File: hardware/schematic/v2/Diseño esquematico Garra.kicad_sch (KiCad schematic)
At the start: 21 parts, among them U2 ESP32-WROOM-32

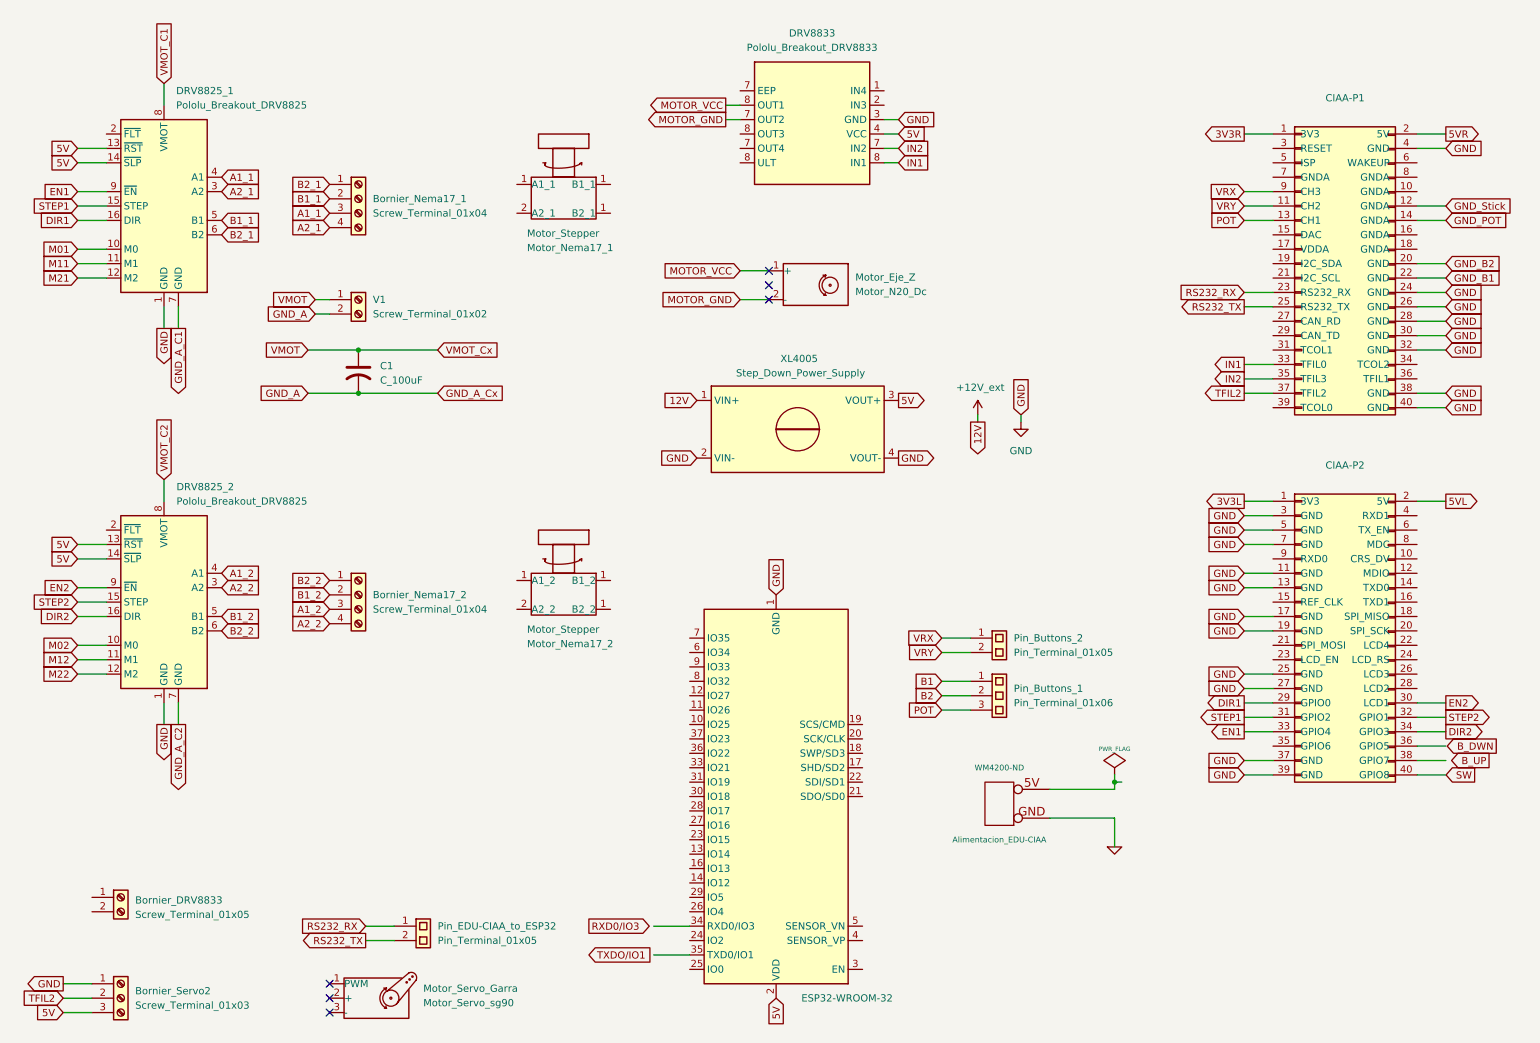
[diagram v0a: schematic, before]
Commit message: Added footprints to Schematic
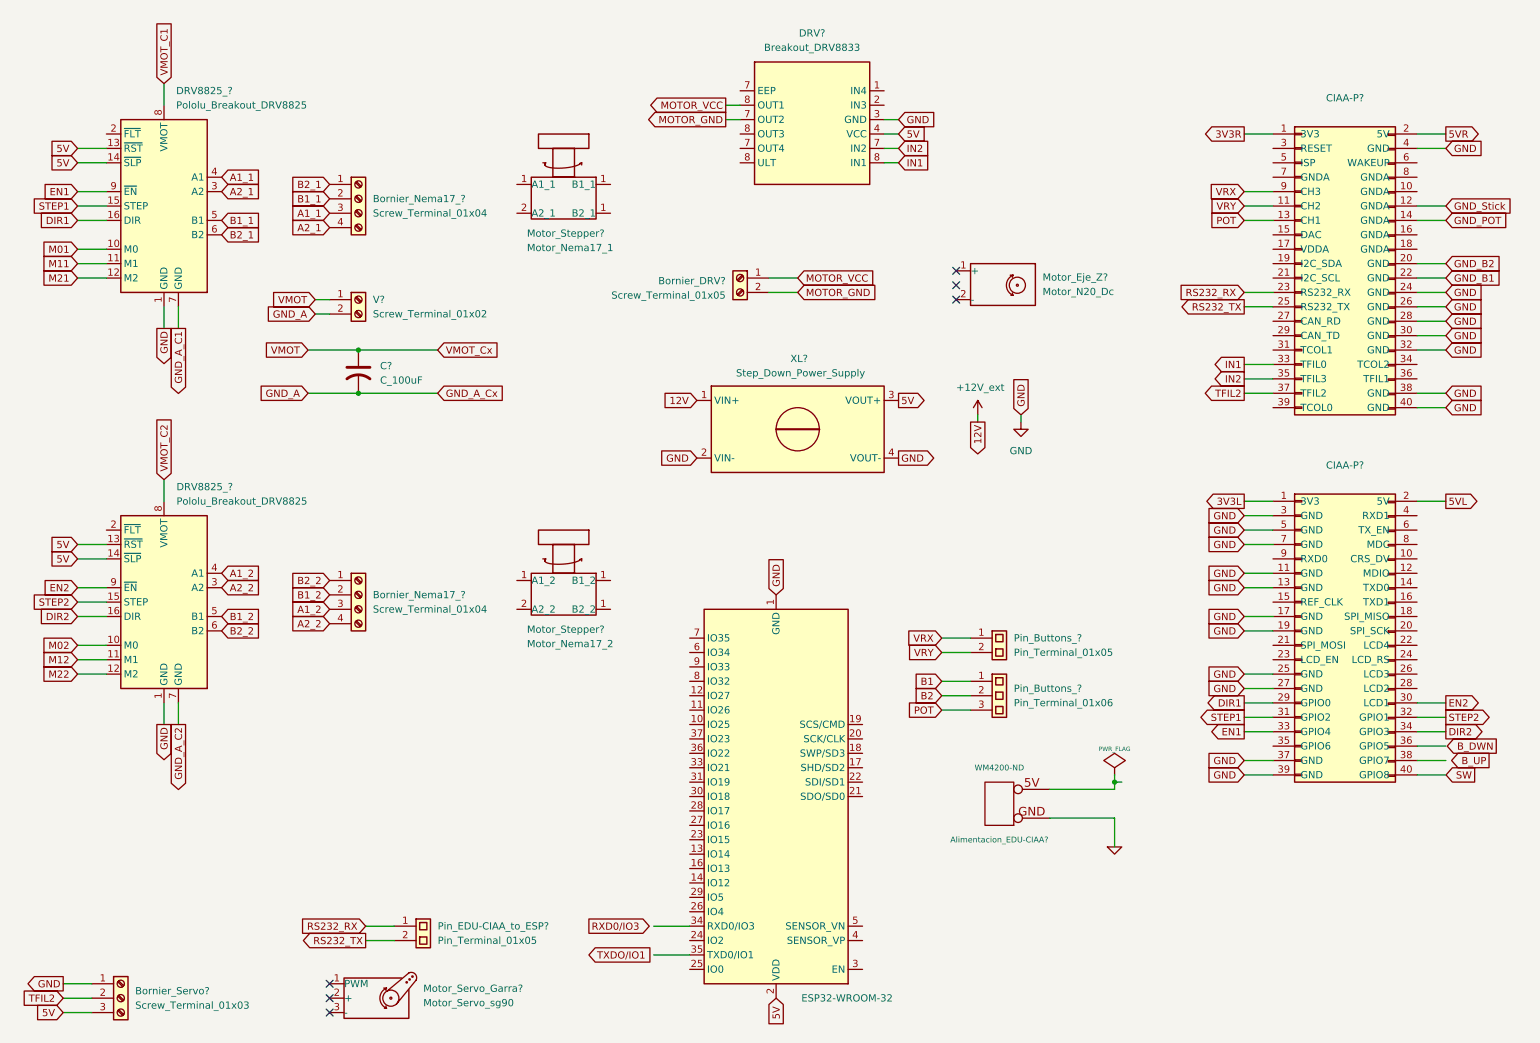
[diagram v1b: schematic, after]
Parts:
- Bornier_DRV?: renamed from Bornier_DRV8833; footprint ProyectoTdL:TerminalBlock_bornier-2_P5.08mm -> TerminalBlock_Phoenix:TerminalBlock_Phoenix_MKDS-1,5-2-5.08_1x02_P5.08mm_Horizontal
- Bornier_Nema17_?: renamed from Bornier_Nema17_1; footprint ProyectoTdL:TerminalBlock_bornier-4_P5.08mm -> TerminalBlock_Phoenix:TerminalBlock_Phoenix_MKDS-1,5-4-5.08_1x04_P5.08mm_Horizontal
- Bornier_Nema17_?: renamed from Bornier_Nema17_2; footprint ProyectoTdL:TerminalBlock_bornier-4_P5.08mm -> TerminalBlock_Phoenix:TerminalBlock_Phoenix_MKDS-1,5-4-5.08_1x04_P5.08mm_Horizontal
- Bornier_Servo?: renamed from Bornier_Servo2; footprint ProyectoTdL:TerminalBlock_bornier-3_P5.08mm -> TerminalBlock_Phoenix:TerminalBlock_Phoenix_MKDS-1,5-3-5.08_1x03_P5.08mm_Horizontal
- C?: renamed from C1; footprint (none) -> Capacitor_THT:C_Radial_D8.0mm_H11.5mm_P3.50mm
- DRV?: renamed from DRV8833; value Pololu_Breakout_DRV8833 -> Breakout_DRV8833
- V?: renamed from V1; footprint ProyectoTdL:TerminalBlock_bornier-2_P5.08mm -> TerminalBlock_Phoenix:TerminalBlock_Phoenix_MKDS-1,5-2-5.08_1x02_P5.08mm_Horizontal
- renumbered Alimentacion_EDU-CIAA to Alimentacion_EDU-CIAA?, CIAA-P1 to CIAA-P?, CIAA-P2 to CIAA-P?, DRV8825_2 to DRV8825_?, DRV8825_1 to DRV8825_?, Motor_Eje_Z to Motor_Eje_Z?, Motor_Servo_Garra to Motor_Servo_Garra?, Motor_Stepper to Motor_Stepper?, Pin_Buttons_2 to Pin_Buttons_?, Pin_Buttons_1 to Pin_Buttons_?, Pin_EDU-CIAA_to_ESP32 to Pin_EDU-CIAA_to_ESP?, U2 to U?, XL4005 to XL?
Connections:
- net MOTOR_GND: now also Bornier_DRV?.2 (Pin_2); no longer Motor_Eje_Z?.2 (-)
- net MOTOR_VCC: now also Bornier_DRV?.1 (Pin_1); no longer Motor_Eje_Z?.1 (+)
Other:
- moved on the sheet: Bornier_DRV?, Motor_Eje_Z?

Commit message: PCB started
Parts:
- removed Alimentacion_EDU-CIAA?: WM4200-ND, ~, symbol edu-ciaa-nxp:CONN_2
- removed Motor_Eje_Z?: Motor_N20_Dc, symbol Motor:Motor_Servo
- removed Motor_Servo_Garra?: Motor_Servo_sg90, symbol Motor:Motor_Servo
- removed Motor_Stepper?: Motor_Nema17_2, symbol Motor:Motor_Servo
- removed Motor_Stepper?: Motor_Nema17_1, symbol Motor:Motor_Servo
- removed U?: ESP32-WROOM-32, RF_Module:ESP32-WROOM-32, symbol RF_Module:ESP32-WROOM-32
- CIAA-P1: renamed from CIAA-P?; footprint ProyectoTdL:Tira_P1_CIAA -> Connector_PinHeader_1.00mm:PinHeader_1x20_P1.00mm_Vertical
- CIAA-P2: renamed from CIAA-P?; footprint ProyectoTdL:Tira_P2_CIAA -> Connector_PinHeader_1.00mm:PinHeader_1x20_P1.00mm_Vertical
- Pin_Buttons_?, Pin_EDU-CIAA_to_ESP?: footprint ProyectoTdL:TerminalBlock_bornier-2_P5.08mm -> Connector_PinSocket_2.00mm:PinSocket_1x02_P2.00mm_Vertical
- Pin_Buttons_?: footprint ProyectoTdL:TerminalBlock_bornier-3_P5.08mm -> Connector_PinSocket_2.00mm:PinSocket_1x03_P2.00mm_Vertical
- gave numbers to parts that had none: 7
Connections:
- net IN1: now also DRV8833.6 (IN1); no longer DRV8833.8 (IN1)
- net IN2: now also DRV8833.5 (IN2); no longer DRV8833.7 (IN2)
- net MOTOR_GND: now also DRV8833.9 (OUT2); no longer DRV8833.7 (IN2)
- no-connect marks 6 -> 0

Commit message: PCB progress
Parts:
- gave numbers to parts that had none: 6
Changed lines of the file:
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@@
 		(dnp no)
 		(fields_autoplaced yes)
-		(property "Reference" "Bornier_Nema17_?"
+		(property "Reference" "Bornier_Nema17_1"
 			(at 82.55 46.9899 0)
 			(effects
@@
 			(project "Diseño esquematico Garra"
 				(path "/a88248f6-7b70-4a9d-b538-4e8e42a3a066"
-					(reference "Bornier_Nema17_?")
+					(reference "Bornier_Nema17_1")
 					(unit 1)
 				)
@@
 		(dnp no)
 		(fields_autoplaced yes)
-		(property "Reference" "Pin_Buttons_?"
+		(property "Reference" "Pin_Buttons_1"
 			(at 195.58 124.4599 0)
 			(effects
@@
 			(project "Diseño esquematico Garra"
 				(path "/a88248f6-7b70-4a9d-b538-4e8e42a3a066"
-					(reference "Pin_Buttons_?")
+					(reference "Pin_Buttons_1")
 					(unit 1)
 				)
@@
 		(dnp no)
 		(fields_autoplaced yes)
-		(property "Reference" "Pin_Buttons_?"
+		(property "Reference" "Pin_Buttons_2"
 			(at 195.58 133.3499 0)
 			(effects
@@
 			(project "Diseño esquematico Garra"
 				(path "/a88248f6-7b70-4a9d-b538-4e8e42a3a066"
-					(reference "Pin_Buttons_?")
+					(reference "Pin_Buttons_2")
 					(unit 1)
 				)
@@
 		(dnp no)
 		(fields_autoplaced yes)
-		(property "Reference" "Bornier_Servo?"
+		(property "Reference" "Bornier_Servo1"
 			(at 40.64 186.6899 0)
 			(effects
@@
 			(project "Diseño esquematico Garra"
 				(path "/a88248f6-7b70-4a9d-b538-4e8e42a3a066"
-					(reference "Bornier_Servo?")
+					(reference "Bornier_Servo1")
 					(unit 1)
 				)
@@
 		(dnp no)
 		(fields_autoplaced yes)
-		(property "Reference" "Pin_EDU-CIAA_to_ESP?"
+		(property "Reference" "Pin_EDU-CIAA_to_ESP1"
 			(at 93.98 175.2599 0)
 			(effects
@@
 			(project "Diseño esquematico Garra"
 				(path "/a88248f6-7b70-4a9d-b538-4e8e42a3a066"
-					(reference "Pin_EDU-CIAA_to_ESP?")
+					(reference "Pin_EDU-CIAA_to_ESP1")
 					(unit 1)
 				)
@@
 		(dnp no)
 		(fields_autoplaced yes)
-		(property "Reference" "Bornier_Nema17_?"
+		(property "Reference" "Bornier_Nema17_2"
 			(at 82.55 116.8399 0)
 			(effects
@@
 			(project "Diseño esquematico Garra"
 				(path "/a88248f6-7b70-4a9d-b538-4e8e42a3a066"
-					(reference "Bornier_Nema17_?")
-					(unit 1)
-				)
+					(reference "Bornier_Nema17_2")
+					(unit 1)
+				)

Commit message: PCB Updated
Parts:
- removed Pin_Buttons_2: Pin_Terminal_01x06, Connector_PinSocket_2.00mm:PinSocket_1x03_P2.00mm_Vertical, symbol Connector:Screw_Terminal_01x03
- added C2: C_100uF, Capacitor_THT:C_Radial_D8.0mm_H11.5mm_P3.50mm, symbol Device:C_US
- added PinOut_B_DWN, PinOut_B_UP, PinOut_POT: Pin_Terminal_01x05, Connector_PinSocket_2.00mm:PinSocket_1x02_P2.00mm_Vertical, symbol Connector:Screw_Terminal_01x02
- CIAA-P1, CIAA-P2: footprint Connector_PinHeader_1.00mm:PinHeader_1x20_P1.00mm_Vertical -> Libreria_EDU_CIAA_NXP:PIN_ARRAY_20X2
- PinOut_Stick: renamed from Pin_Buttons_1; footprint Connector_PinSocket_2.00mm:PinSocket_1x02_P2.00mm_Vertical -> Connector_PinSocket_2.00mm:PinSocket_1x04_P2.00mm_Vertical
- renumbered Pin_EDU-CIAA_to_ESP1 to PinOut_UART, V1 to V_Input
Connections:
- net GND_A is gone; now on net GND: C1.2, V_Input.2 (Pin_2)
- net GND_A_C1 is gone; now on net GND: DRV8825_1.7 (GND)
- net GND_A_C2 is gone; now on net GND: DRV8825_2.7 (GND)
- net VMOT is gone; now on net +12V_ext: C1.1, V_Input.1 (Pin_1)
- net VMOT_C1 is gone; now on net +12V_ext: DRV8825_1.8 (VMOT)
- net VMOT_C2 is gone; now on net +12V_ext: DRV8825_2.8 (VMOT)
- net +12V_ext: now also C2.1
- net B_DWN: now also PinOut_B_DWN.1 (Pin_1)
- net B_UP: now also PinOut_B_UP.1 (Pin_1)
- net GND: now also C2.2
- net GND_POT: now also PinOut_POT.2 (Pin_2)
- net GND_Stick: now also PinOut_Stick.3 (Pin_3)
- net POT: now also PinOut_POT.1 (Pin_1)
- net SW: now also PinOut_Stick.4 (Pin_4)
- net GND_B1 renamed GND_B_DWN
- net GND_B_DWN: now also PinOut_B_DWN.2 (Pin_2)
- net GND_B2 renamed GND_B_UP
- net GND_B_UP: now also PinOut_B_UP.2 (Pin_2)
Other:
- moved on the sheet: Bornier_Servo1, CIAA-P1, CIAA-P2, PinOut_UART

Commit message: PCB updated
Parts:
- renumbered Bornier_DRV8833 to Bornier_DRV1, DRV8833 to DRV1, PinOut_UART to PinOut_UART1, V_Input to V_Input1
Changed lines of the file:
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@@
 		(dnp no)
 		(fields_autoplaced yes)
-		(property "Reference" "#PWR0102"
+		(property "Reference" "#PWR02"
 			(at 196.85 92.71 0)
 			(effects
@@
 			(project "Diseño esquematico Garra"
 				(path "/a88248f6-7b70-4a9d-b538-4e8e42a3a066"
-					(reference "#PWR0102")
+					(reference "#PWR02")
 					(unit 1)
 				)
@@
 		(on_board yes)
 		(dnp no)
-		(property "Reference" "#PWR0101"
+		(property "Reference" "#PWR01"
 			(at 189.23 88.9 0)
 			(effects
@@
 			(project "Diseño esquematico Garra"
 				(path "/a88248f6-7b70-4a9d-b538-4e8e42a3a066"
-					(reference "#PWR0101")
+					(reference "#PWR01")
 					(unit 1)
 				)
@@
 		(on_board yes)
 		(dnp no)
-		(property "Reference" "Bornier_DRV8833"
+		(property "Reference" "Bornier_DRV1"
 			(at 144.78 61.468 0)
 			(effects
@@
 			(project "Diseño esquematico Garra"
 				(path "/a88248f6-7b70-4a9d-b538-4e8e42a3a066"
-					(reference "Bornier_DRV8833")
+					(reference "Bornier_DRV1")
 					(unit 1)
 				)
@@
 		(fields_autoplaced yes)
 		(property "Reference" "PinOut_Stick"
-			(at 195.58 133.3499 0)
+			(at 195.58 135.8899 0)
 			(effects
 				(font
@@
 		)
 		(property "Value" "Pin_Terminal_01x05"
-			(at 195.58 135.8899 0)
+			(at 195.58 138.4299 0)
 			(effects
 				(font
@@
 		(dnp no)
 		(fields_autoplaced yes)
-		(property "Reference" "DRV8833"
+		(property "Reference" "DRV1"
 			(at 160.02 17.78 0)
 			(effects
@@
 			(project "Diseño esquematico Garra"
 				(path "/a88248f6-7b70-4a9d-b538-4e8e42a3a066"
-					(reference "DRV8833")
+					(reference "DRV1")
 					(unit 1)
 				)
@@
 		(dnp no)
 		(fields_autoplaced yes)
-		(property "Reference" "PinOut_UART"
+		(property "Reference" "PinOut_UART1"
 			(at 196.85 49.5299 0)
 			(effects
@@
 			(project "Diseño esquematico Garra"
 				(path "/a88248f6-7b70-4a9d-b538-4e8e42a3a066"
-					(reference "PinOut_UART")
+					(reference "PinOut_UART1")
 					(unit 1)
 				)
@@
 		(dnp no)
 		(fields_autoplaced yes)
-		(property "Reference" "V_Input"
+		(property "Reference" "V_Input1"
 			(at 82.55 64.7699 0)
 			(effects
@@
 			(project "Diseño esquematico Garra"
 				(path "/a88248f6-7b70-4a9d-b538-4e8e42a3a066"
-					(reference "V_Input")
-					(unit 1)
-				)
+					(reference "V_Input1")
+					(unit 1)
+				)

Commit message: PCB Updated
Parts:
- renumbered Bornier_DRV1 to Bornier_N20_DC, DRV1 to DRV833, PinOut_B_DWN to PinOut_B_DWN1, PinOut_B_UP to PinOut_B_UP1, PinOut_POT to PinOut_POT1, PinOut_Stick to PinOut_Stick1
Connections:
- net +12V_ext: now also DRV8825_1.16 (VMOT), DRV8825_2.16 (VMOT); no longer DRV8825_1.8 (VMOT), DRV8825_2.8 (VMOT)
- net 5V: now also DRV833.9 (VCC), DRV8825_1.5 (~{RST}), DRV8825_1.6 (~{SLP}), DRV8825_2.5 (~{RST}), DRV8825_2.6 (~{SLP}); no longer DRV833.4 (VCC), DRV8825_1.13 (~{RST}), DRV8825_1.14 (~{SLP}), DRV8825_2.13 (~{RST}), DRV8825_2.14 (~{SLP})
- net A1_1: now also Bornier_Nema17_1.2 (Pin_2), DRV8825_1.12 (A1); no longer Bornier_Nema17_1.3 (Pin_3), DRV8825_1.4 (A1)
- net A1_2: now also Bornier_Nema17_2.2 (Pin_2), DRV8825_2.12 (A1); no longer Bornier_Nema17_2.3 (Pin_3), DRV8825_2.4 (A1)
- net A2_1: now also Bornier_Nema17_1.1 (Pin_1), DRV8825_1.11 (A2); no longer Bornier_Nema17_1.4 (Pin_4), DRV8825_1.3 (A2)
- net A2_2: now also Bornier_Nema17_2.1 (Pin_1), DRV8825_2.11 (A2); no longer Bornier_Nema17_2.4 (Pin_4), DRV8825_2.3 (A2)
- net B1_1: now also Bornier_Nema17_1.3 (Pin_3), DRV8825_1.13 (B1); no longer Bornier_Nema17_1.2 (Pin_2), DRV8825_1.5 (B1)
- net B1_2: now also Bornier_Nema17_2.3 (Pin_3), DRV8825_2.13 (B1); no longer Bornier_Nema17_2.2 (Pin_2), DRV8825_2.5 (B1)
- net B2_1: now also Bornier_Nema17_1.4 (Pin_4), DRV8825_1.14 (B2); no longer Bornier_Nema17_1.1 (Pin_1), DRV8825_1.6 (B2)
- net B2_2: now also Bornier_Nema17_2.4 (Pin_4), DRV8825_2.14 (B2); no longer Bornier_Nema17_2.1 (Pin_1), DRV8825_2.6 (B2)
- net DIR1: now also DRV8825_1.8 (DIR); no longer DRV8825_1.16 (DIR)
- net DIR2: now also DRV8825_2.8 (DIR); no longer DRV8825_2.16 (DIR)
- net EN1: now also DRV8825_1.1 (~{EN}); no longer DRV8825_1.9 (~{EN})
- net EN2: now also DRV8825_2.1 (~{EN}); no longer DRV8825_2.9 (~{EN})
- net GND: now also DRV833.10 (GND), DRV8825_1.15 (GND), DRV8825_1.9 (GND), DRV8825_2.15 (GND), DRV8825_2.9 (GND); no longer DRV833.3 (GND), DRV8825_1.1 (GND), DRV8825_1.7 (GND), DRV8825_2.1 (GND), DRV8825_2.7 (GND)
- net IN1: now also DRV833.7 (IN1); no longer DRV833.6 (IN1)
- net IN2: now also DRV833.8 (IN2); no longer DRV833.5 (IN2)
- net M01: now also DRV8825_1.2 (M0); no longer DRV8825_1.10 (M0)
- net M02: now also DRV8825_2.2 (M0); no longer DRV8825_2.10 (M0)
- net M11: now also DRV8825_1.3 (M1); no longer DRV8825_1.11 (M1)
- net M12: now also DRV8825_2.3 (M1); no longer DRV8825_2.11 (M1)
- net M21: now also DRV8825_1.4 (M2); no longer DRV8825_1.12 (M2)
- net M22: now also DRV8825_2.4 (M2); no longer DRV8825_2.12 (M2)
- net MOTOR_GND: now also DRV833.3 (OUT2); no longer DRV833.9 (OUT2)
- net MOTOR_VCC: now also DRV833.2 (OUT1); no longer DRV833.8 (OUT1)
- net STEP1: now also DRV8825_1.7 (STEP); no longer DRV8825_1.15 (STEP)
- net STEP2: now also DRV8825_2.7 (STEP); no longer DRV8825_2.15 (STEP)
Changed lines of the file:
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@@
 		)
 	)
-	(global_label "A2_2"
+	(global_label "B2_2"
 		(shape input)
 		(at 74.93 121.92 180)
@@
 		)
 	)
-	(global_label "A1_1"
+	(global_label "B1_1"
 		(shape input)
 		(at 74.93 49.53 180)
@@
 		)
 	)
-	(global_label "B1_1"
+	(global_label "A1_1"
 		(shape input)
 		(at 74.93 46.99 180)
@@
 		)
 	)
-	(global_label "B1_2"
+	(global_label "A1_2"
 		(shape input)
 		(at 74.93 116.84 180)
@@
 		)
 	)
-	(global_label "B2_1"
+	(global_label "A2_1"
 		(shape input)
 		(at 74.93 44.45 180)
@@
 		)
 	)
-	(global_label "A2_1"
+	(global_label "B2_1"
 		(shape input)
 		(at 74.93 52.07 180)
@@
 		)
 	)
-	(global_label "A1_2"
+	(global_label "B1_2"
 		(shape input)
 		(at 74.93 119.38 180)
@@
 		)
 	)
-	(global_label "B2_2"
+	(global_label "A2_2"
 		(shape input)
 		(at 74.93 114.3 180)
@@
 		(dnp no)
 		(fields_autoplaced yes)
-		(property "Reference" "PinOut_POT"
+		(property "Reference" "PinOut_POT1"
 			(at 195.58 126.9999 0)
 			(effects
@@
 			(project "Diseño esquematico Garra"
 				(path "/a88248f6-7b70-4a9d-b538-4e8e42a3a066"
-					(reference "PinOut_POT")
+					(reference "PinOut_POT1")
 					(unit 1)
 				)
@@
 	)
 	(symbol
-		(lib_name "Screw_Terminal_01x02_1")
+		(lib_name "Screw_Terminal_01x02_4")
 		(lib_id "Connector:Screw_Terminal_01x02")
 		(at 193.04 114.3 0)
@@
 		(dnp no)
 		(fields_autoplaced yes)
-		(property "Reference" "PinOut_B_DWN"
+		(property "Reference" "PinOut_B_DWN1"
 			(at 195.58 114.2999 0)
 			(effects
@@
 			(project "Diseño esquematico Garra"
 				(path "/a88248f6-7b70-4a9d-b538-4e8e42a3a066"
-					(reference "PinOut_B_DWN")
+					(reference "PinOut_B_DWN1")
 					(unit 1)
 				)
@@
 	)
 	(symbol
+		(lib_name "Pololu_Breakout_DRV8825_3")
 		(lib_id "Driver_Motor:Pololu_Breakout_DRV8825")
 		(at 45.72 45.72 0)
@@
 		)
 		(property "Datasheet" "https://www.pololu.com/product/2982"
-			(at 48.26 53.34 0)
+			(at 47.752 78.74 0)
 			(effects
 				(font
@@
 		)
 		(property "Description" "Pololu Breakout Board, Stepper Driver DRV8825"
-			(at 45.72 45.72 0)
+			(at 47.498 76.454 0)
 			(effects
 				(font
@@
 		(pin "10"
 		)
+		(pin "7"
+		)
+		(pin "5"
+		)
 		(pin "9"
-		)
-		(pin "5"
-		)
-		(pin "7"
 		)
 		(instances
@@
 		(on_board yes)
 		(dnp no)
-		(property "Reference" "Bornier_DRV1"
+		(property "Reference" "Bornier_N20_DC"
 			(at 144.78 61.468 0)
 			(effects
@@
 			(project "Diseño esquematico Garra"
 				(path "/a88248f6-7b70-4a9d-b538-4e8e42a3a066"
-					(reference "Bornier_DRV1")
+					(reference "Bornier_N20_DC")
 					(unit 1)
 				)
@@
 		(dnp no)
 		(fields_autoplaced yes)
-		(property "Reference" "PinOut_Stick"
+		(property "Reference" "PinOut_Stick1"
 			(at 195.58 135.8899 0)
 			(effects
@@
 			(project "Diseño esquematico Garra"
 				(path "/a88248f6-7b70-4a9d-b538-4e8e42a3a066"
-					(reference "PinOut_Stick")
+					(reference "PinOut_Stick1")
 					(unit 1)
 				)
@@
 	)
 	(symbol
-		(lib_name "Screw_Terminal_01x02_1")
+		(lib_name "Screw_Terminal_01x02_5")
 		(lib_id "Connector:Screw_Terminal_01x02")
 		(at 193.04 120.65 0)
@@
 		(dnp no)
 		(fields_autoplaced yes)
-		(property "Reference" "PinOut_B_UP"
+		(property "Reference" "PinOut_B_UP1"
 			(at 195.58 120.6499 0)
 			(effects
@@
 			(project "Diseño esquematico Garra"
 				(path "/a88248f6-7b70-4a9d-b538-4e8e42a3a066"
-					(reference "PinOut_B_UP")
+					(reference "PinOut_B_UP1")
 					(unit 1)
 				)
@@
 		(dnp no)
 		(fields_autoplaced yes)
-		(property "Reference" "DRV1"
+		(property "Reference" "DRV833"
 			(at 160.02 17.78 0)
 			(effects
@@
 			(project "Diseño esquematico Garra"
 				(path "/a88248f6-7b70-4a9d-b538-4e8e42a3a066"
-					(reference "DRV1")
+					(reference "DRV833")
 					(unit 1)
 				)
@@
 	)
 	(symbol
-		(lib_name "Screw_Terminal_01x02_1")
+		(lib_name "Screw_Terminal_01x02_3")
 		(lib_id "Connector:Screw_Terminal_01x02")
 		(at 194.31 49.53 0)
